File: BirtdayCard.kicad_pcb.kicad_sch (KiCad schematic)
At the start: 30 parts, among them Q3 G2312, U1 ESP32-C3-WROOM-02-N4(4MB), U2 0.763V~7V 4.2V~18V 3A

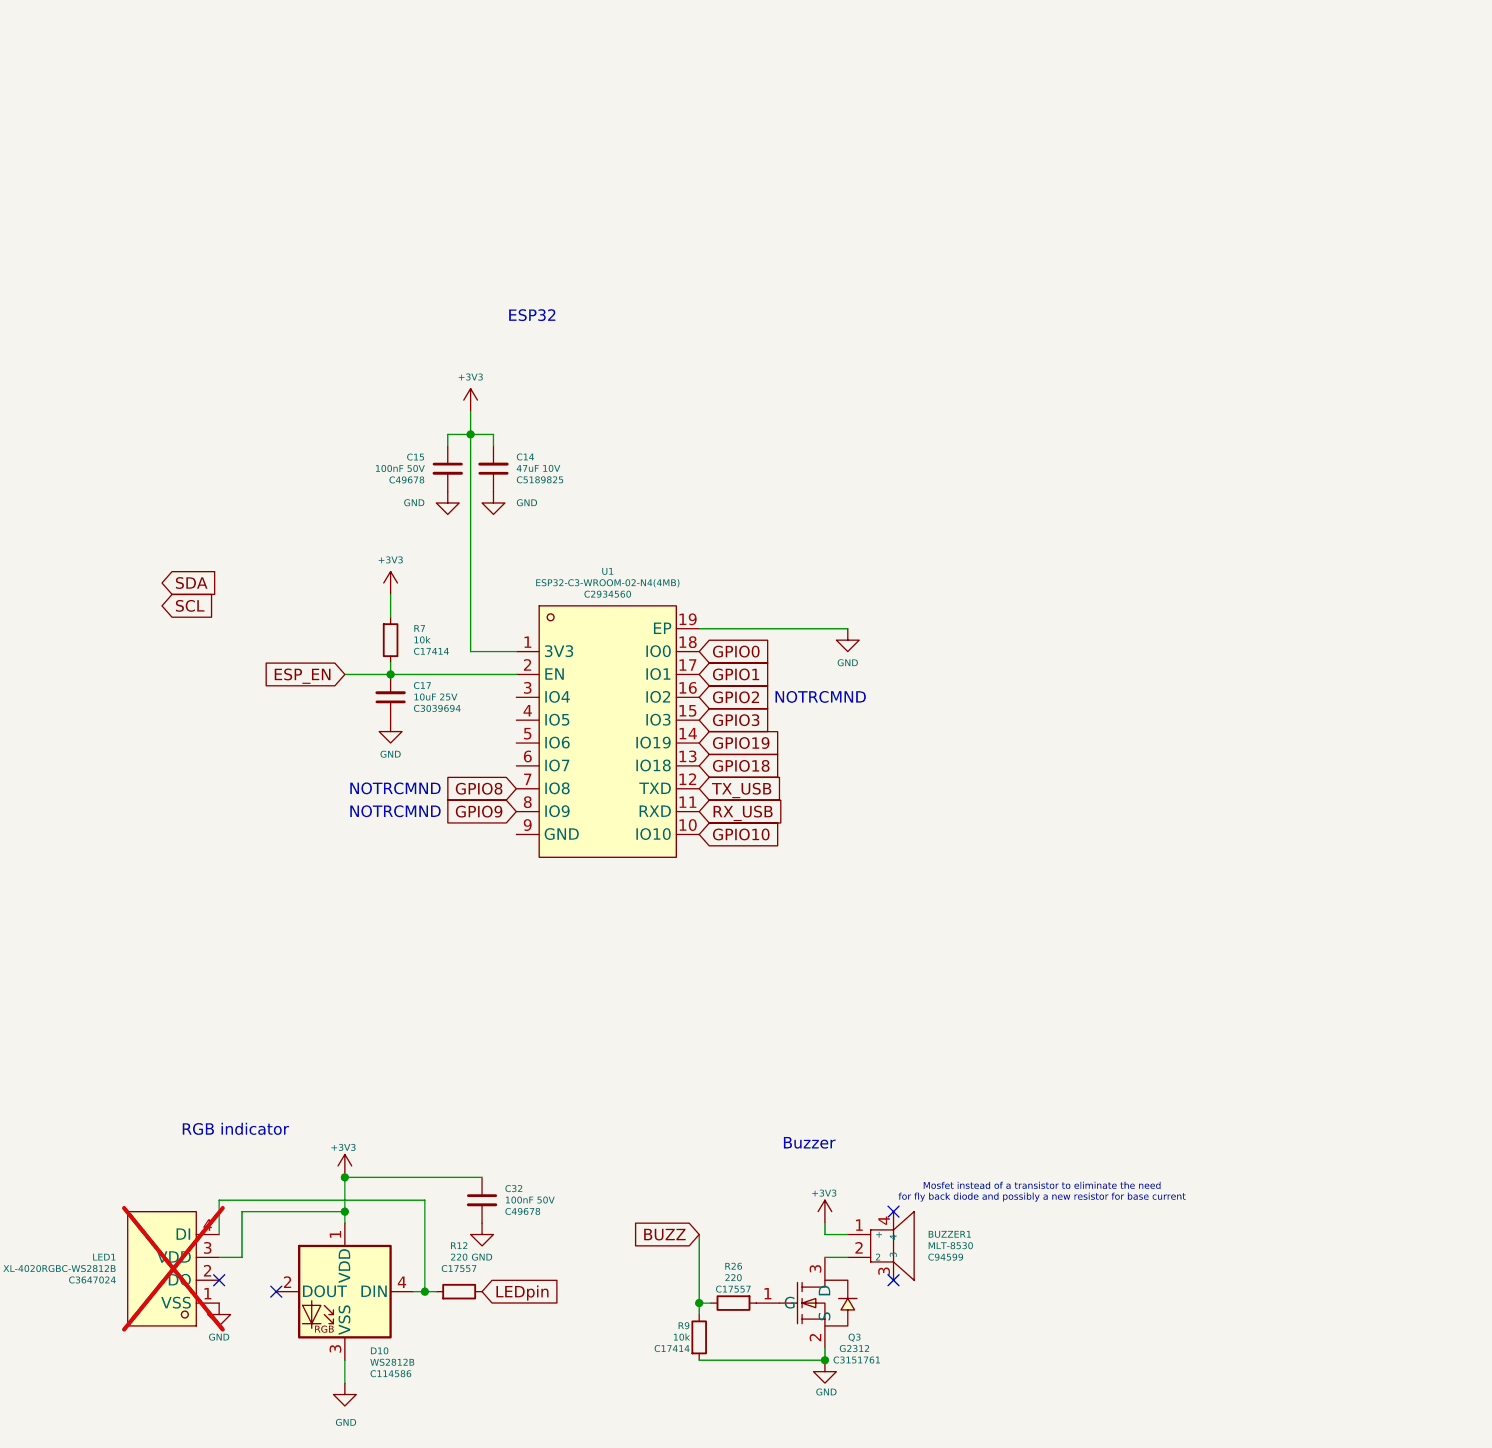
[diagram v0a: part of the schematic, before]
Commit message: Pin configurations ESP32
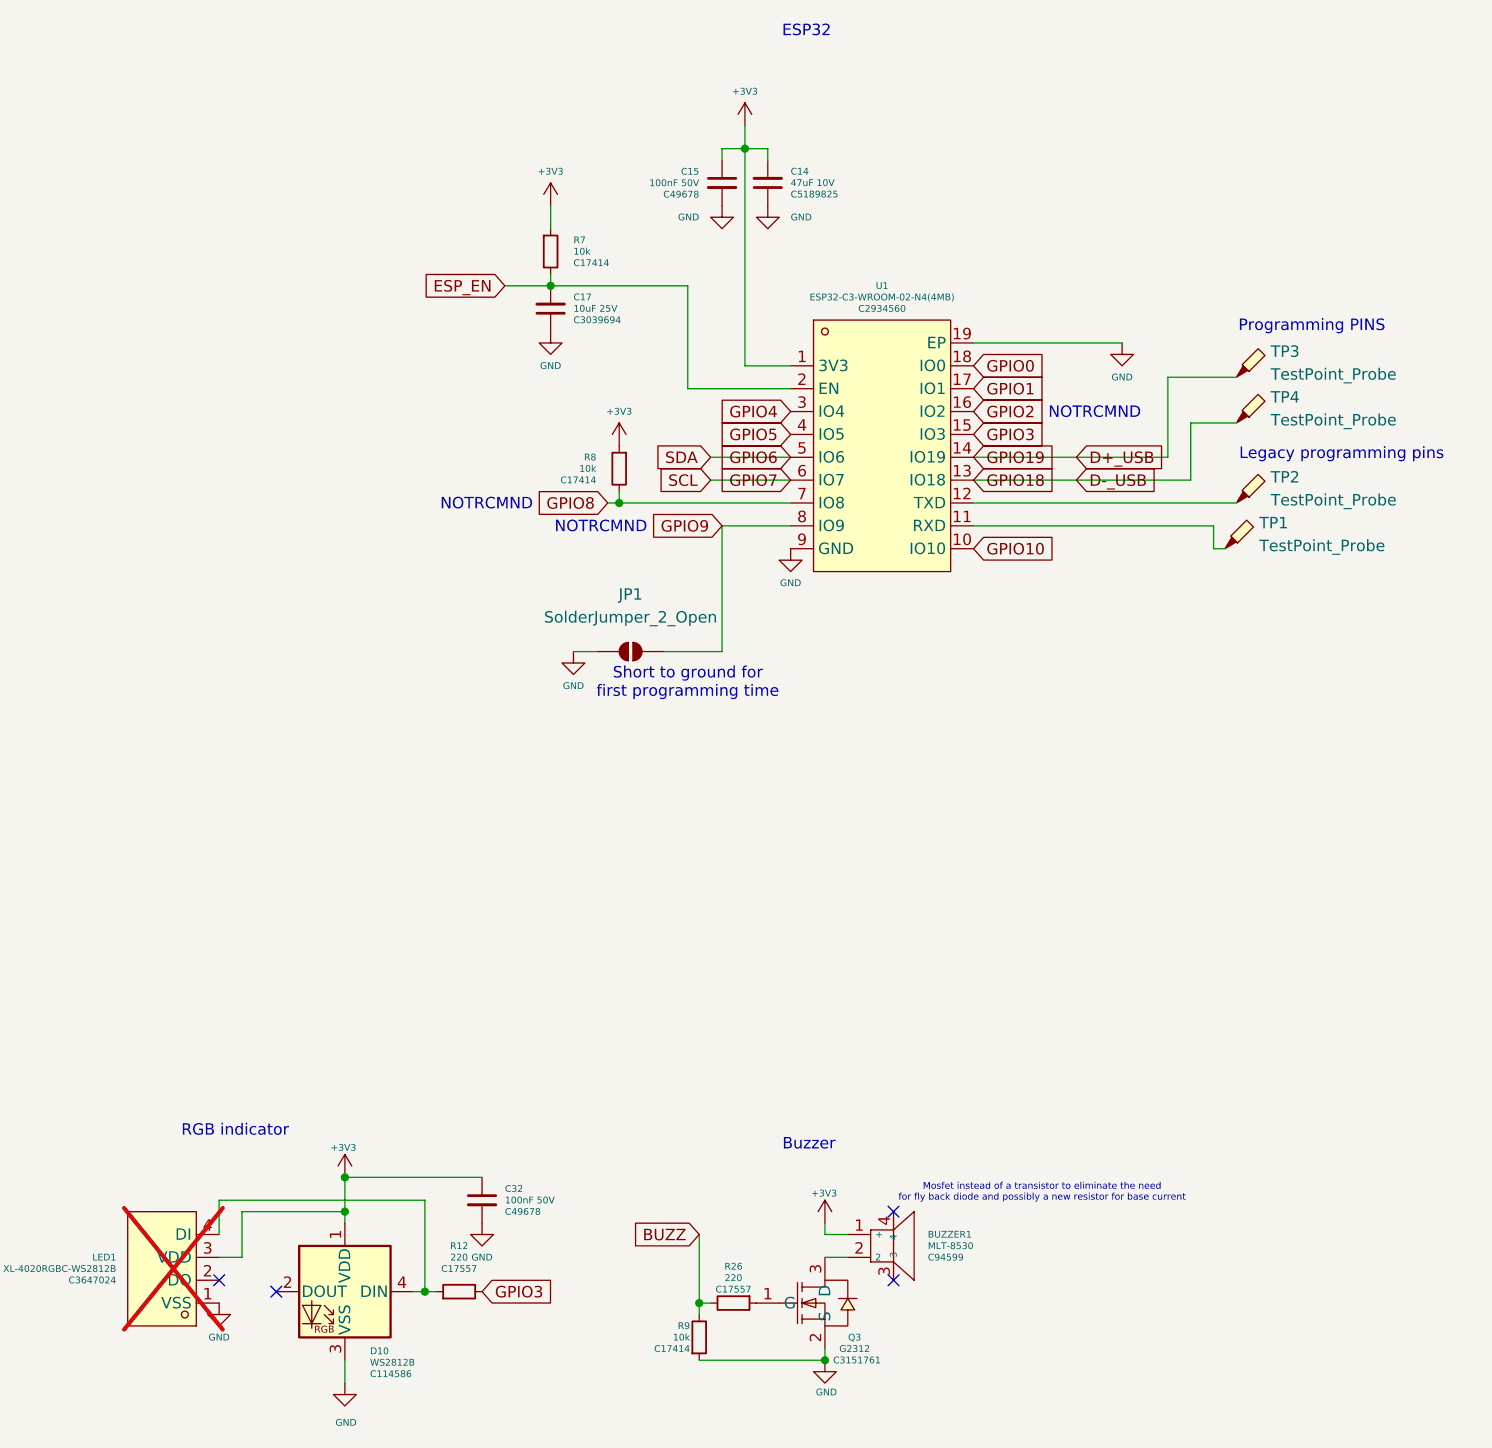
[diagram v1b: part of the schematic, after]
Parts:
- added JP1: SolderJumper_2_Open, symbol Jumper:SolderJumper_2_Open
- added R8: 10k, Resistor_SMD:R_0805_2012Metric_Pad1.20x1.40mm_HandSolder, symbol Device:R_Small
- added TP1, TP2, TP3, TP4: TestPoint_Probe, symbol Connector:TestPoint_Probe
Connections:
- net LEDpin is gone; now on net GPIO3: R12.2
- net SCL is gone; now on net GPIO7: D5.1 (A1), R14.1
- net SDA is gone; now on net GPIO6: D5.2 (A2), R15.1
- net +3V3: now also R8.1
- net GND: now also U1.9 (GND), JP1.1 (A)
- net GPIO8: now also R8.2
- net GPIO9: now also JP1.2 (B)
- net GPIO4: now reaches U1.3 (IO4)
- net GPIO5: now reaches U1.4 (IO5)
- net GPIO6: now reaches U1.5 (IO6)
- net GPIO7: now reaches U1.6 (IO7)
- net GPIO18 renamed D-_USB
- net D-_USB: now also TP4.1
- net GPIO19 renamed D+_USB
- net D+_USB: now also TP3.1
- net RX_USB: no longer names the net of U1.11 (RXD)
- net RX_USB: now also TP1.1
- net TX_USB: no longer names the net of U1.12 (TXD)
- net TX_USB: now also TP2.1
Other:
- note added: "Legacy programming pins"
- note added: "Programming PINS"
- note added: "Short to ground for first programming time"
- moved on the sheet: C14, C15, C17, R7, U1

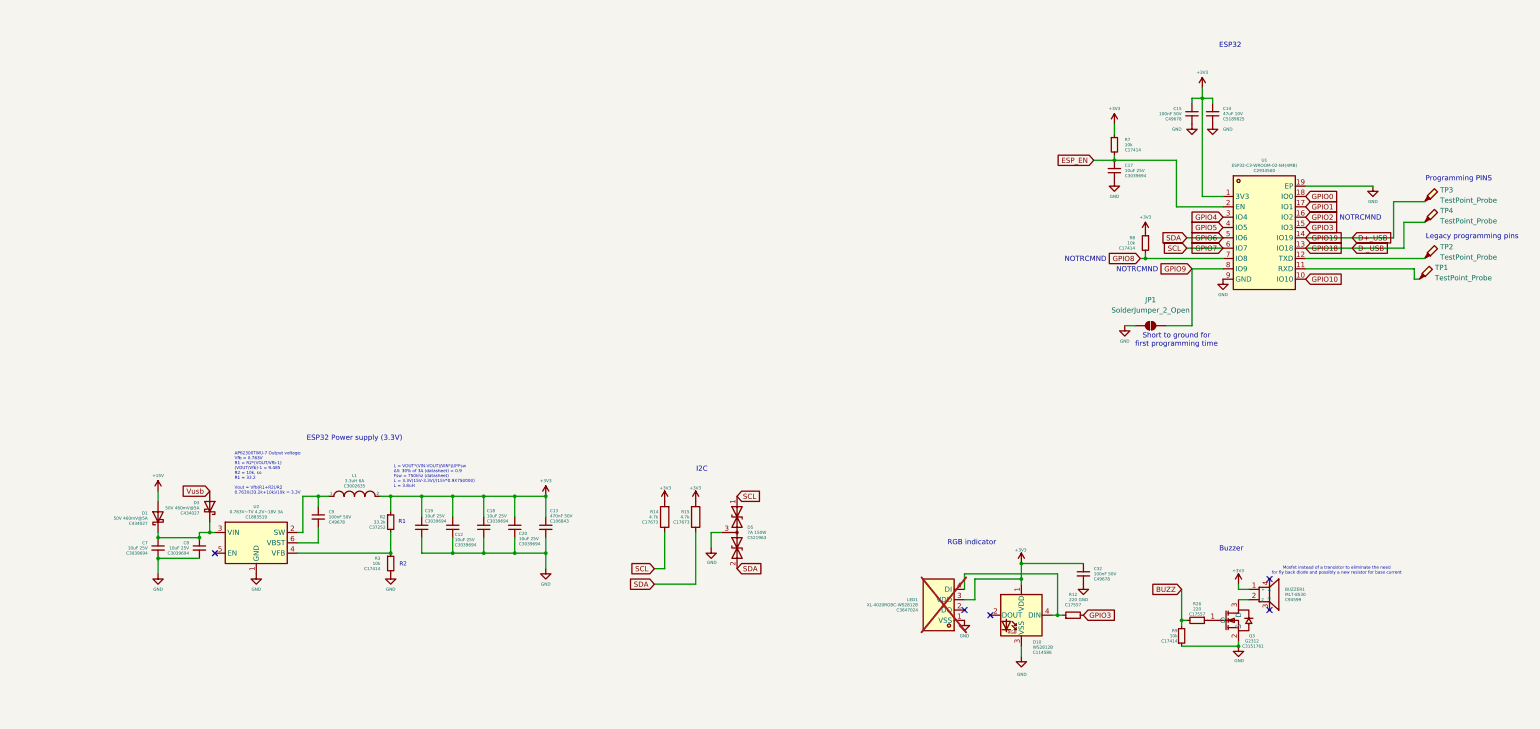
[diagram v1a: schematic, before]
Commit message: adding components and consolidating with current parts
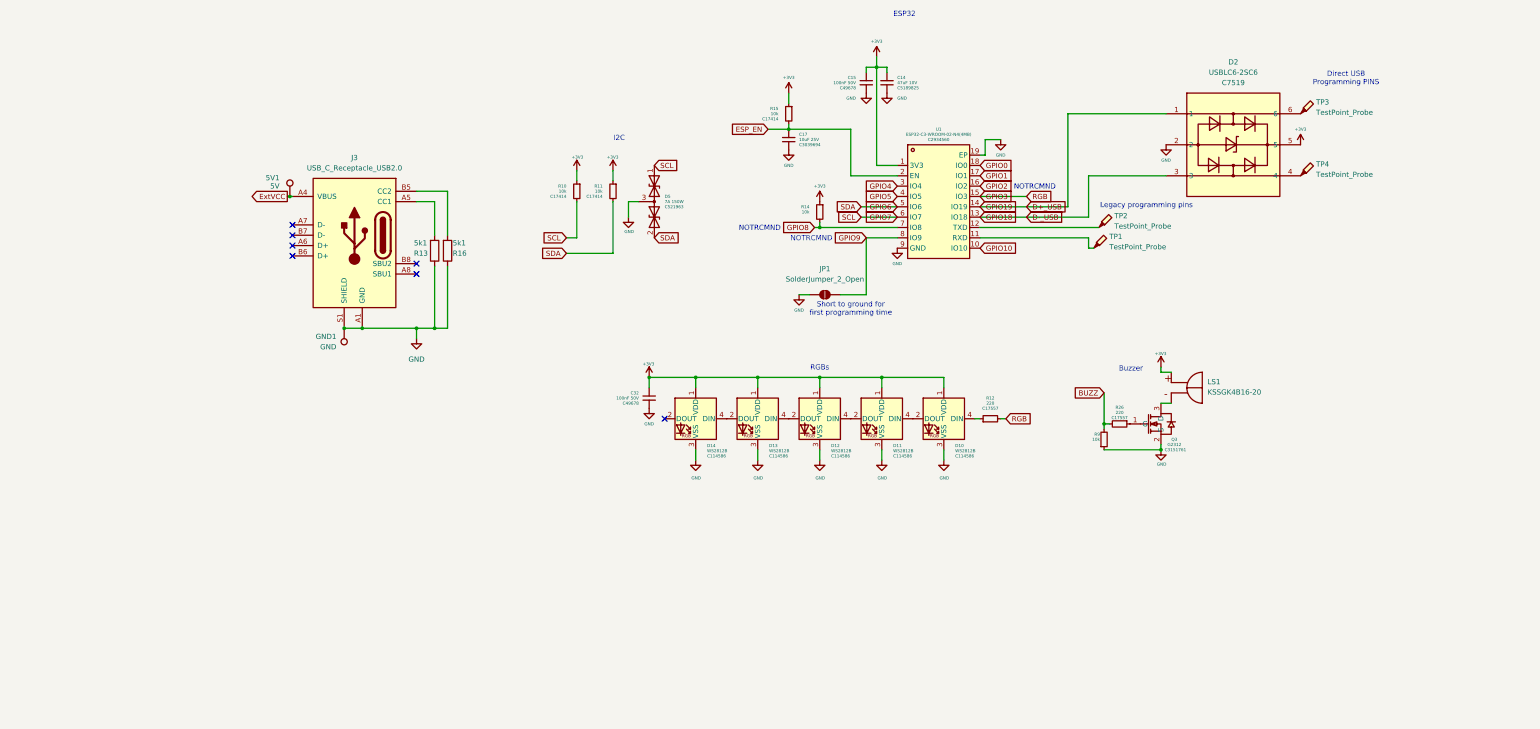
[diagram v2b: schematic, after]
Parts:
- removed BUZZER1: MLT-8530, VolstoraEasyEda:BUZ-SMD_4P-L8.5-W8.5-P8.50-BR, symbol VolstoraEasyEda:MLT-8530
- removed C12, C18, C19, C20, C7, C8: 10uF 25V, Capacitor_SMD:C_0805_2012Metric_Pad1.18x1.45mm_HandSolder, symbol Device:C_Small
- removed C13: 470nF 50V, Capacitor_SMD:C_0805_2012Metric_Pad1.18x1.45mm_HandSolder, symbol Device:C_Small
- removed C9: 100nF 50V, Capacitor_SMD:C_0805_2012Metric_Pad1.18x1.45mm_HandSolder, symbol Device:C_Small
- removed D1, D3: 50V 460mV@5A, VolstoraEasyEda:SMA_L4.4-W2.6-LS5.0-RD, symbol Device:D_Schottky
- removed L1: 3.3uH 6A, Inductor_SMD:L_Bourns_SRP7028A_7.3x6.6mm, symbol Titan_frontplate_front_BMS_V1.3-rescue:INDUCTOR-pspice
- removed LED1: XL-4020RGBC-WS2812B, VolstoraEasyEda:LED-SMD_4P-L4.0-W1.7_XL-4020RGBC-WS2812B, symbol VolstoraEasyEda:XL-4020RGBC-WS2812B
- removed R14, R15: 4.7k, Resistor_SMD:R_0805_2012Metric_Pad1.20x1.40mm_HandSolder, symbol Device:R
- removed R2: 33.2k, Resistor_SMD:R_0805_2012Metric_Pad1.20x1.40mm_HandSolder, symbol Device:R_Small
- removed R3, R7, R8: 10k, Resistor_SMD:R_0805_2012Metric_Pad1.20x1.40mm_HandSolder, symbol Device:R_Small
- removed U2: 0.763V~7V 4.2V~18V 3A, Package_TO_SOT_SMD:TSOT-23-6, symbol Titan_frontplate_front_BMS_V1.3-rescue:AP62300-Regulator_Switching
- added 5V1: 5V, TestPoint:TestPoint_Pad_1.0x1.0mm, symbol Connector:TestPoint
- added D11, D12, D13, D14: WS2812B, VolstoraEasyEda:LED-SMD_4P-L5.0-W5.0-BL_TC5050RGB, symbol LED:WS2812B
- added D2: USBLC6-2SC6, easyeda2kicad:SOT-23-6_L2.9-W1.6-P0.95-LS2.8-BL, symbol easyeda2kicad:USBLC6-2SC6
- added GND1: GND, TestPoint:TestPoint_Pad_1.0x1.0mm, symbol Connector:TestPoint
- added J3: USB_C_Receptacle_USB2.0, USB-C-Power-tester:TYPE-C-31-M-17_handsolder, symbol Connector:USB_C_Receptacle_USB2.0
- added LS1: KSSGK4B16-20, Snapeda:XDCR_KSSGK4B16-20, symbol KSSGK4B16-20:KSSGK4B16-20
- added R10, R11, R14, R15: 10k, Resistor_SMD:R_1206_3216Metric_Pad1.30x1.75mm_HandSolder, symbol Device:R_Small
- added R13, R16: 5k1, Resistor_SMD:R_1206_3216Metric_Pad1.30x1.75mm_HandSolder, symbol Device:R
- R12, R9: footprint Resistor_SMD:R_0805_2012Metric_Pad1.20x1.40mm_HandSolder -> Resistor_SMD:R_1206_3216Metric_Pad1.30x1.75mm_HandSolder
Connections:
- net +3V3: now also D11.1 (VDD), D12.1 (VDD), D13.1 (VDD), D14.1 (VDD), D2.5, LS1.P, R10.1, R11.1, R14.1, R15.1
- net D+_USB: now also D2.1; no longer TP3.1
- net D-_USB: now also D2.3; no longer TP4.1
- net ESP_EN: now also R15.2
- net GND: now also D11.3 (VSS), D12.3 (VSS), D13.3 (VSS), D14.3 (VSS), D2.2, GND1.1, J3.A1 (GND), J3.A12 (GND), J3.B1 (GND), J3.B12 (GND), J3.S1 (SHIELD), R13.1, R16.1
- net GPIO6: now also R11.2
- net GPIO7: now also R10.2
- net GPIO8: now also R14.2
- net at D10.2 (DOUT): now also D11.4 (DIN)
- net at Q3.3 (D): now also LS1.N
- new net: D2.4, TP4.1
- new net: J3.B5 (CC2), R16.2
- new net: D2.6, TP3.1
- new net: J3.A5 (CC1), R13.2
- new net: D12.2 (DOUT), D13.4 (DIN)
- new net: D11.2 (DOUT), D12.4 (DIN)
- new net: D13.2 (DOUT), D14.4 (DIN)
- new net ExtVCC: 5V1.1, J3.A4 (VBUS), J3.A9 (VBUS), J3.B4 (VBUS), J3.B9 (VBUS)
- no-connect marks 5 -> 7
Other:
- note added: "Direct USB Programming PINS"
- note added: "RGBs"
- note removed: "AP62300TWU-7 Output voltage: Vfb = 0.763V R1 = R2*(VOUT/Vfb-1) (VOUT/Vfb)-1 = 9.485 R2 = 10k, so R1 = 33.2 Vout = Vfb(R1+R2)/R2 0.763X(33.2k+10k)/10k = 3.3V"
- note removed: "ESP32 Power supply (3.3V)"
- note removed: "L = VOUT*(VIN-VOUT)/VIN*ΔIl*Fsw ΔIl: 30% of 3A (datasheet) = 0.9 Fsw = 750khz (datasheet) L = 3.3V(15V-3.3V)/(15V*0.9X750000) L = 3.8uH"
- note removed: "Mosfet instead of a transistor to eliminate the need for fly back diode and possibly a new resistor for base current"
- note removed: "Programming PINS"
- note removed: "R1"
- note removed: "R2"
- note removed: "RGB indicator"
- moved on the sheet: C14, C15, C17, C32, D10, D5, JP1, Q3, R12, R26, R9, TP1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
